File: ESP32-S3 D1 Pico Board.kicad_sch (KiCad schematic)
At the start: 2 parts

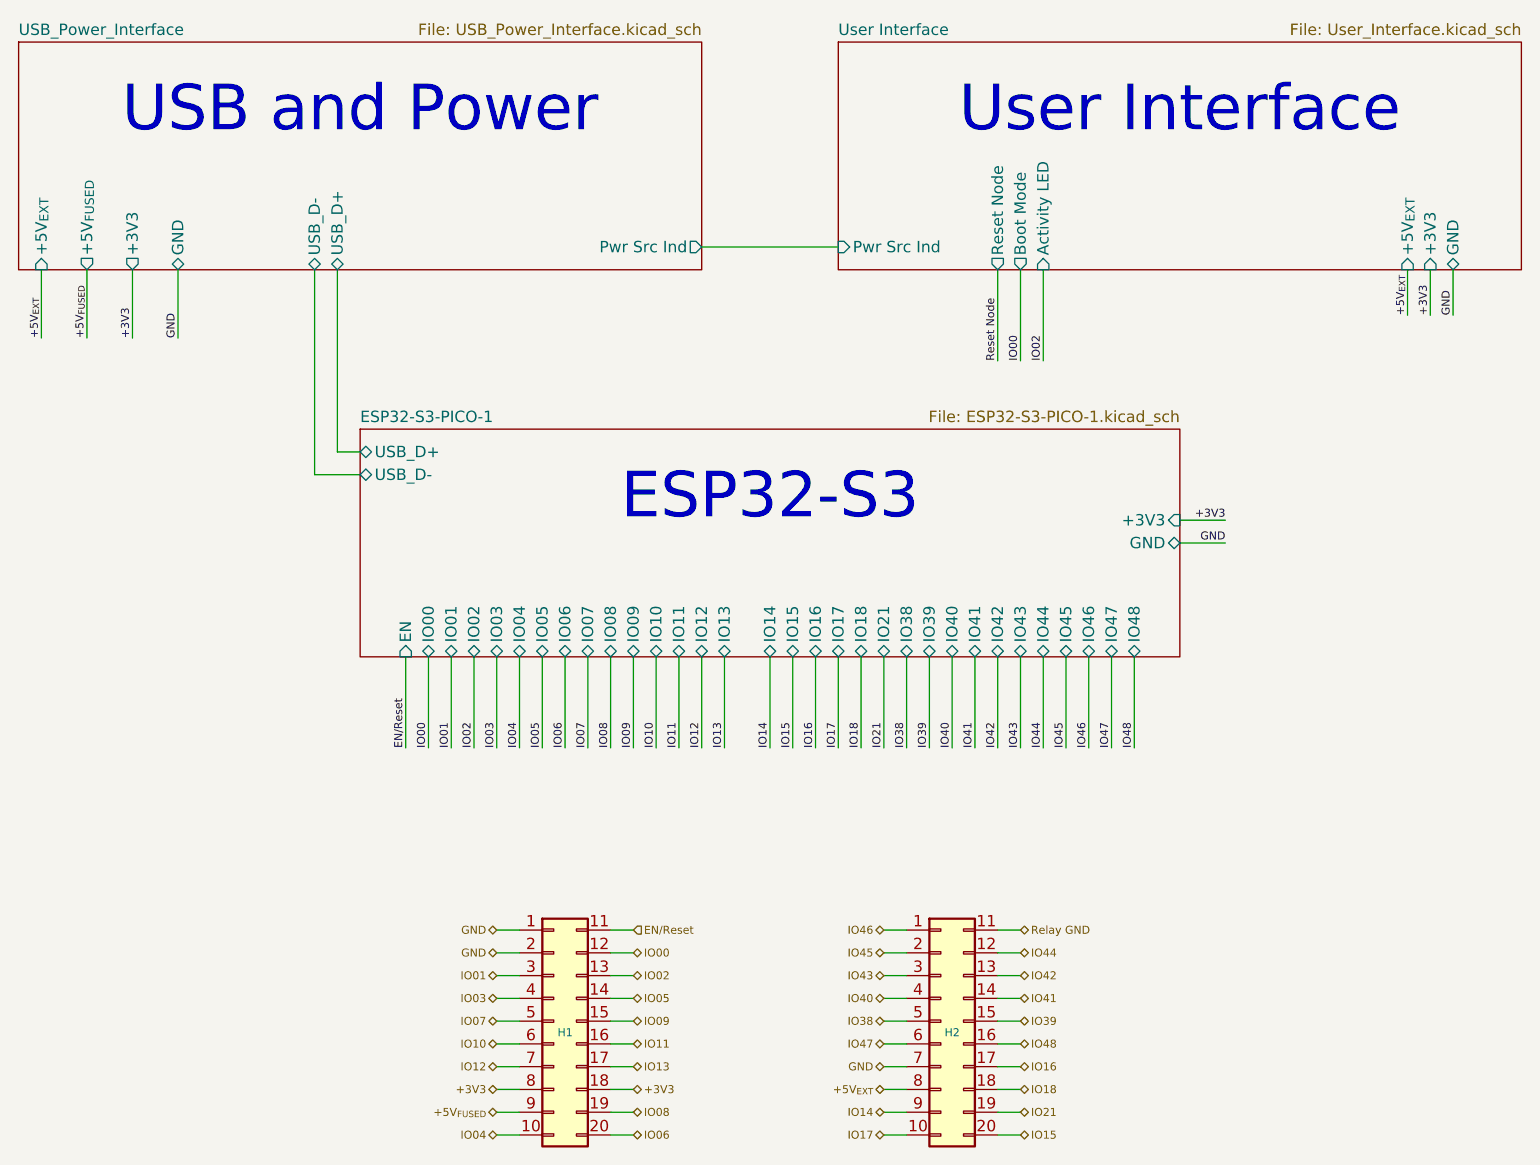
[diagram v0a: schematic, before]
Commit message: Update CANBus_Interface.kicad_sch, ESP32-S3 D1 Pico Board.kicad_sch, ESP32-S3 Pico D1.kicad_pcb, and 15 more files
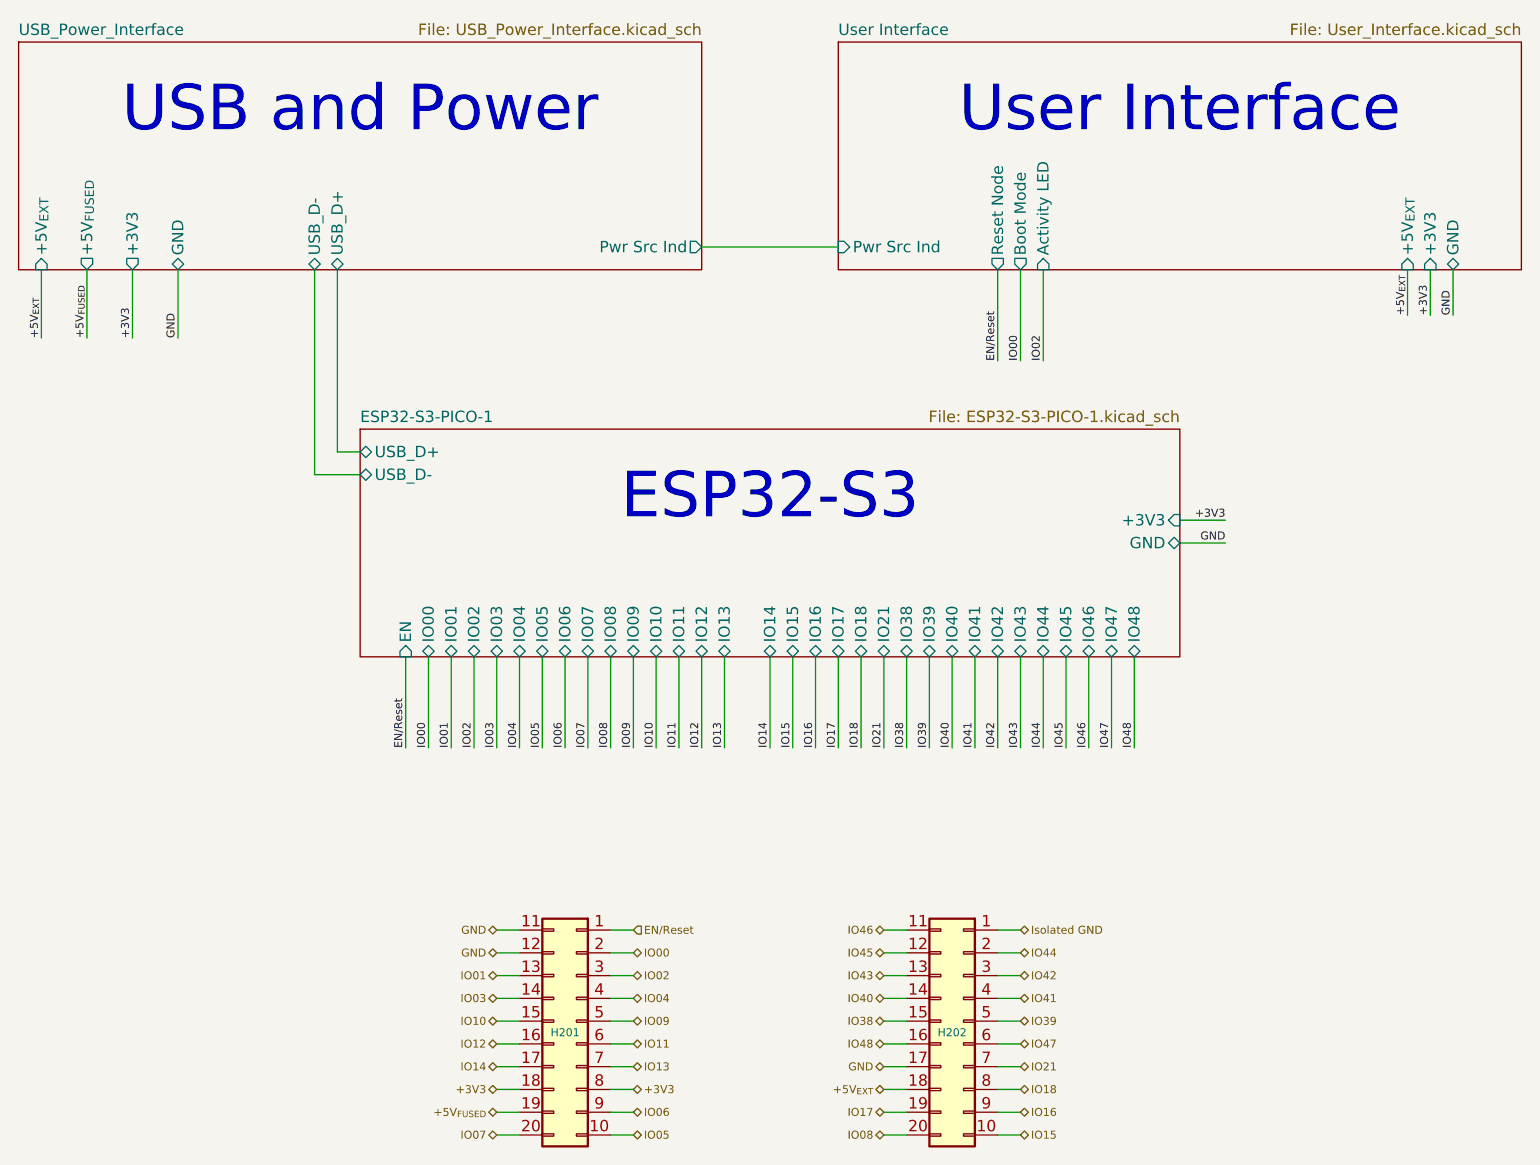
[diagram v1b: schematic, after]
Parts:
- H201: renamed from H1; footprint Personal_FootprintLibrary:PinHeader_2x10_P2.54mm_Vertical_BottomMount_TopReference -> My Connectors:PinHeader_2x10_P2.54mm_Vertical_THT_BottomMount_TopReference
- H202: renamed from H2; footprint Personal_FootprintLibrary:PinHeader_2x10_P2.54mm_Vertical_BottomMount_TopReference -> My Connectors:PinHeader_2x10_P2.54mm_Vertical_THT_BottomMount_TopReference
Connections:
- net Relay GND is gone; now on net IO46: H202.11 (Pin_11)
- net +5V_{EXT}: now also H202.18 (Pin_18); no longer H202.8 (Pin_8)
- net +5V_{FUSED}: now also H201.19 (Pin_19); no longer H201.9 (Pin_9)
- net EN/Reset: now also H201.1 (Pin_1); no longer H201.11 (Pin_11)
- net GND: now also H201.11 (Pin_11), H201.12 (Pin_12), H202.17 (Pin_17); no longer H201.1 (Pin_1), H201.2 (Pin_2), H202.7 (Pin_7)
- net IO00: now also H201.2 (Pin_2); no longer H201.12 (Pin_12)
- net IO01: now also H201.13 (Pin_13); no longer H201.3 (Pin_3)
- net IO02: now also H201.3 (Pin_3); no longer H201.13 (Pin_13)
- net IO03: now also H201.14 (Pin_14); no longer H201.4 (Pin_4)
- net IO04: now also H201.4 (Pin_4); no longer H201.10 (Pin_10)
- net IO05: now also H201.10 (Pin_10); no longer H201.14 (Pin_14)
- net IO06: now also H201.9 (Pin_9); no longer H201.20 (Pin_20)
- net IO07: now also H201.20 (Pin_20); no longer H201.5 (Pin_5)
- net IO08: now also H202.20 (Pin_20); no longer H201.19 (Pin_19)
- net IO09: now also H201.5 (Pin_5); no longer H201.15 (Pin_15)
- net IO10: now also H201.15 (Pin_15); no longer H201.6 (Pin_6)
- net IO11: now also H201.6 (Pin_6); no longer H201.16 (Pin_16)
- net IO12: now also H201.16 (Pin_16); no longer H201.7 (Pin_7)
- net IO13: now also H201.7 (Pin_7); no longer H201.17 (Pin_17)
- net IO14: now also H201.17 (Pin_17); no longer H202.9 (Pin_9)
- net IO15: now also H202.10 (Pin_10); no longer H202.20 (Pin_20)
- net IO16: now also H202.9 (Pin_9); no longer H202.17 (Pin_17)
- net IO17: now also H202.19 (Pin_19); no longer H202.10 (Pin_10)
- net IO18: now also H202.8 (Pin_8); no longer H202.18 (Pin_18)
- net IO21: now also H202.7 (Pin_7); no longer H202.19 (Pin_19)
- net IO38: now also H202.15 (Pin_15); no longer H202.5 (Pin_5)
- net IO39: now also H202.5 (Pin_5); no longer H202.15 (Pin_15)
- net IO40: now also H202.14 (Pin_14); no longer H202.4 (Pin_4)
- net IO41: now also H202.4 (Pin_4); no longer H202.14 (Pin_14)
- net IO42: now also H202.3 (Pin_3); no longer H202.13 (Pin_13)
- net IO43: now also H202.13 (Pin_13); no longer H202.3 (Pin_3)
- net IO44: now also H202.2 (Pin_2); no longer H202.12 (Pin_12)
- net IO45: now also H202.12 (Pin_12); no longer H202.2 (Pin_2)
- net IO46: no longer H202.1 (Pin_1)
- new net Isolated GND: H202.1 (Pin_1)

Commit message: Update CAN_Interface.kicad_sch, ESP32-S3 D1 Pico Board.kicad_sch, ESP32-S3 Pico D1.kicad_pcb, and 5 more files
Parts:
- H201, H202: symbol PersonalSchematicSymbolLibrary:Conn_02x10_Top_Bottom_MountingPin -> PersonalSchematicSymbolLibrary:Conn_02x10_Top_Bottom; now in the parts list
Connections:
- net EN/Reset renamed EN/~{Reset}
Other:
- sheet ESP32-S3-PICO-1 ports: added EN/~{RST}; removed EN
- sheet User Interface ports: added ~{Reset Node}; removed Reset Node
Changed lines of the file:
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@@
 		)
 	)
-	(label "EN{slash}Reset"
+	(label "EN{slash}~{Reset}"
 		(at 172.72 60.96 90)
 		(effects
@@
 		)
 	)
-	(label "EN{slash}Reset"
+	(label "EN{slash}~{Reset}"
 		(at 106.68 104.14 90)
 		(effects
@@
 		)
 	)
-	(hierarchical_label "EN{slash}Reset"
+	(hierarchical_label "EN{slash}~{Reset}"
 		(shape input)
 		(at 132.08 124.46 0)
@@
 	)
 	(symbol
-		(lib_id "PersonalSchematicSymbolLibrary:Conn_02x10_Top_Bottom_MountingPin")
+		(lib_id "PersonalSchematicSymbolLibrary:Conn_02x10_Top_Bottom")
 		(at 170.18 124.46 0)
 		(mirror y)
 		(unit 1)
 		(exclude_from_sim no)
-		(in_bom no)
+		(in_bom yes)
 		(on_board yes)
 		(dnp no)
@@
 		)
 		(property "Footprint" "My Connectors:PinHeader_2x10_P2.54mm_Vertical_THT_BottomMount_TopReference"
-			(at 170.18 154.94 0)
-			(effects
-				(font
-					(size 1.27 1.27)
-				)
-				(justify left bottom)
+			(at 171.45 123.19 0)
+			(effects
+				(font
+					(size 1.27 1.27)
+				)
 				(hide yes)
 			)
@@
 		)
 		(property "Description" "Generic connectable mounting pin connector, double row, 02x10, top/bottom pin numbering scheme (row 1: 1...pins_per_row, row2: pins_per_row+1 ... num_pins), script generated (kicad-library-utils/schlib/autogen/connector/)"
-			(at 170.18 157.48 0)
-			(effects
-				(font
-					(size 1.27 1.27)
-				)
-				(justify left bottom)
+			(at 170.18 141.224 0)
+			(effects
+				(font
+					(size 1.27 1.27)
+				)
 				(hide yes)
 			)
@@
 	)
 	(symbol
-		(lib_id "PersonalSchematicSymbolLibrary:Conn_02x10_Top_Bottom_MountingPin")
+		(lib_id "PersonalSchematicSymbolLibrary:Conn_02x10_Top_Bottom")
 		(at 127 124.46 0)
 		(mirror y)
 		(unit 1)
 		(exclude_from_sim no)
-		(in_bom no)
+		(in_bom yes)
 		(on_board yes)
 		(dnp no)
@@
 		)
 		(property "Footprint" "My Connectors:PinHeader_2x10_P2.54mm_Vertical_THT_BottomMount_TopReference"
-			(at 123.19 161.798 0)
+			(at 128.27 123.19 0)
 			(effects
 				(font
@@
 		)
 		(property "Description" "Generic connectable mounting pin connector, double row, 02x10, top/bottom pin numbering scheme (row 1: 1...pins_per_row, row2: pins_per_row+1 ... num_pins), script generated (kicad-library-utils/schlib/autogen/connector/)"
-			(at 104.14 157.988 0)
+			(at 127 141.224 0)
 			(effects
 				(font
@@
 			)
 		)
-		(pin "EN" input
+		(pin "EN{slash}~{RST}" input
 			(at 106.68 93.98 270)
 			(effects
@@
 			)
 		)
-		(pin "Reset Node" output
+		(pin "~{Reset Node}" output
 			(at 172.72 50.8 270)
 			(effects
